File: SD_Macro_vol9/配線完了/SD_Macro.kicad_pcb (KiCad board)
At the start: 2 copper layers, 191.9 x 136.1 mm, 101 parts, among them J1 TRRS_MJ-4PP-9, SW1 SW_PUSH, SW10 SW_PUSH, SW11 SW_PUSH, SW12 SW_PUSH, SW13 SW_PUSH, SW14 SW_PUSH, SW15 SW_PUSH, SW16 SW_PUSH, SW17 SW_PUSH, SW18 SW_PUSH, SW19 SW_PUSH, SW2 SW_PUSH, SW20 SW_PUSH, SW21 SW_PUSH, SW22 SW_PUSH, SW23 Rotary_Encoder_Switch, SW24 SW_PUSH, SW25 SW_PUSH, SW26 SW_PUSH, SW27 SW_PUSH, SW28 SW_PUSH, SW29 SW_PUSH, SW3 SW_PUSH, SW30 SW_PUSH, SW31 SW_PUSH, SW32 SW_PUSH, SW33 SW_PUSH, SW34 SW_PUSH, SW4 SW_PUSH, SW5 SW_PUSH, SW6 SW_PUSH, SW7 SW_PUSH, SW8 SW_PUSH, SW9 SW_PUSH, U1 ProMicro

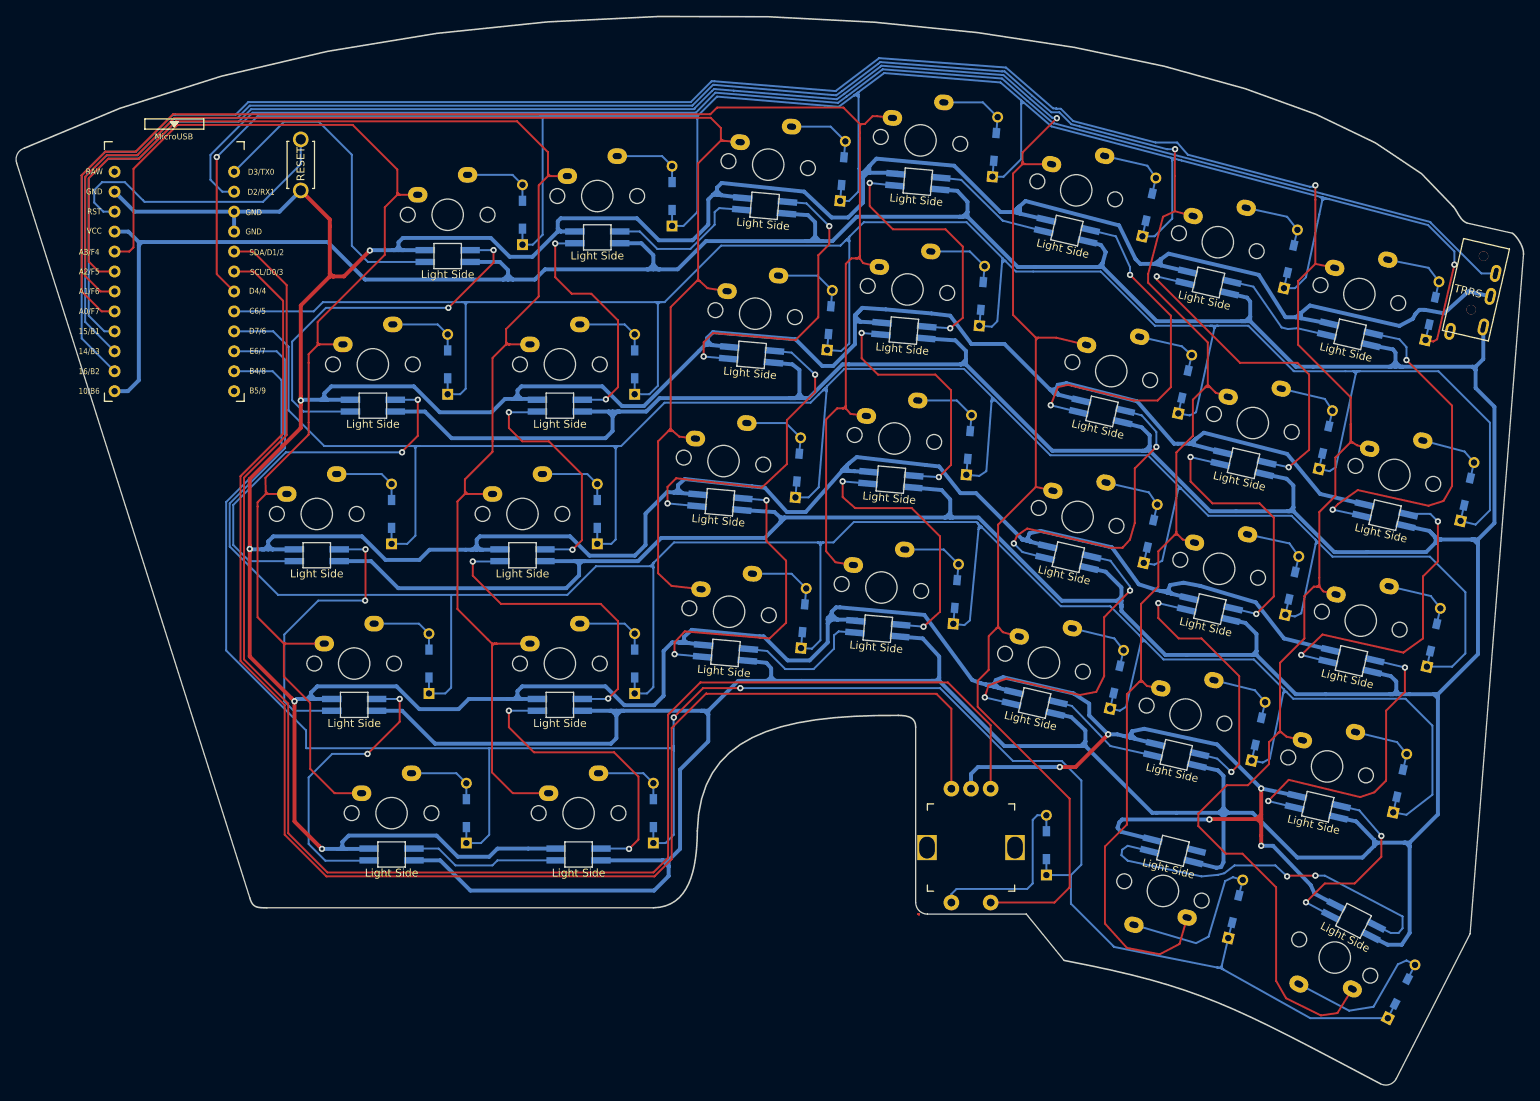
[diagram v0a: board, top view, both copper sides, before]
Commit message: ProMicro の表裏を変更
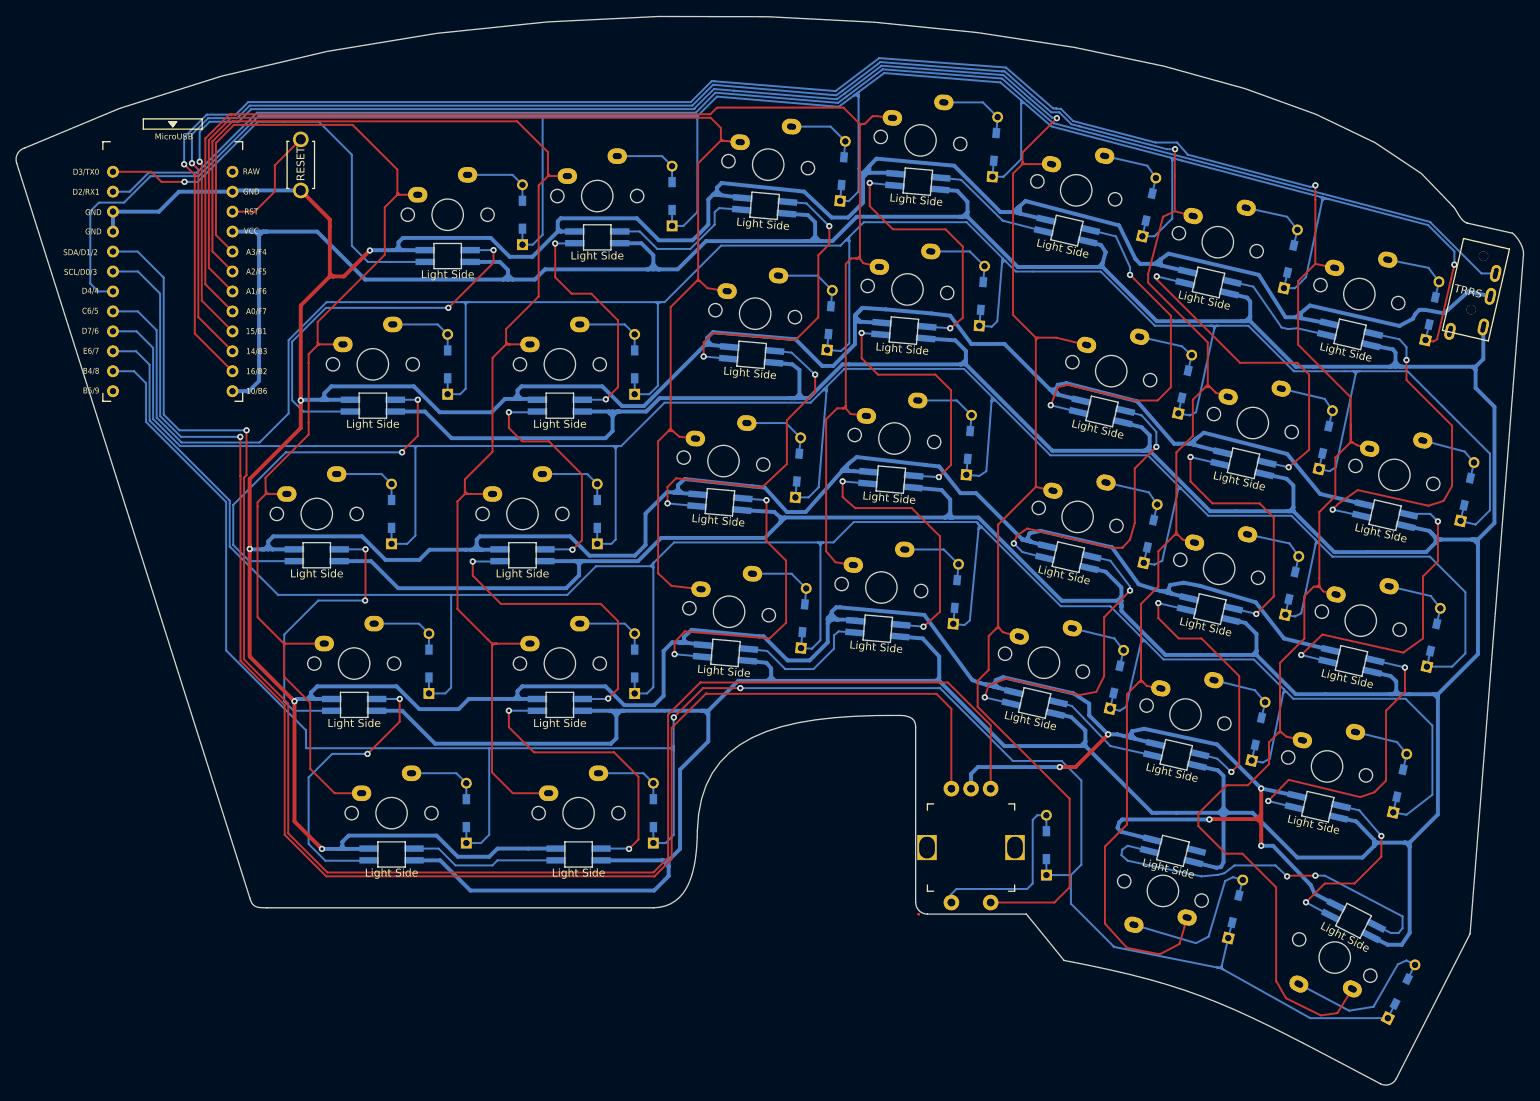
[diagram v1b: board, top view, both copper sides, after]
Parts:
- SW1, SW11, SW12, SW13, SW14, SW15, SW16, SW17, SW18, SW19, SW20, SW21, SW22, SW24, SW25, SW26, SW27, SW28, SW29, SW30, SW31, SW32, SW6, SW7, SW8, SW9: footprint kbd_SW:CherryMX_1u_solder -> kbd_SW:CherryMX_1u_solder_plateless
- SW10, SW33, SW5: footprint kbd_SW:CherryMX_1.25u_solder -> kbd_SW:CherryMX_1.25u_solder_plateless
- SW2: footprint kbd_SW:CherryMX_1.5u_solder -> kbd_SW:CherryMX_1.5u_solder_plateless
- SW3, SW4: footprint kbd_SW:CherryMX_1.75u_solder -> kbd_SW:CherryMX_1.75u_solder_plateless
- U1: footprint kbd:ProMicro_v3.5 -> kbd:ProMicro_v3.5_rev2
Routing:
- net Row1: track 295.3 -> 334.2 mm
- net Reset: track 37.6 -> 14.5 mm
- net LED: track 41.5 -> 58.0 mm, vias 0 -> 1
- net Row2: track 297.9 -> 313.9 mm
- net Col1: track 187.6 -> 173.1 mm
- net Col2: track 179.6 -> 165.2 mm
- net Col3: track 197.1 -> 182.8 mm
- net Row0: track 326.0 -> 339.4 mm, vias 2 -> 1
- net VCC: track 1047.4 -> 1035.6 mm
- net Col4: track 290.2 -> 279.1 mm, vias 1 -> 2
- net Col5: track 307.9 -> 298.1 mm, vias 1 -> 2
- net Col0: track 160.5 -> 150.7 mm
- net Col6: track 342.4 -> 332.8 mm, vias 1 -> 2
- net RotaryA: track 205.4 -> 213.0 mm, vias 0 -> 1
- net Data: track 181.8 -> 189.3 mm
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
